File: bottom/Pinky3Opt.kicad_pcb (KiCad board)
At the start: 2 copper layers, 136 x 102.7 mm, 4 parts

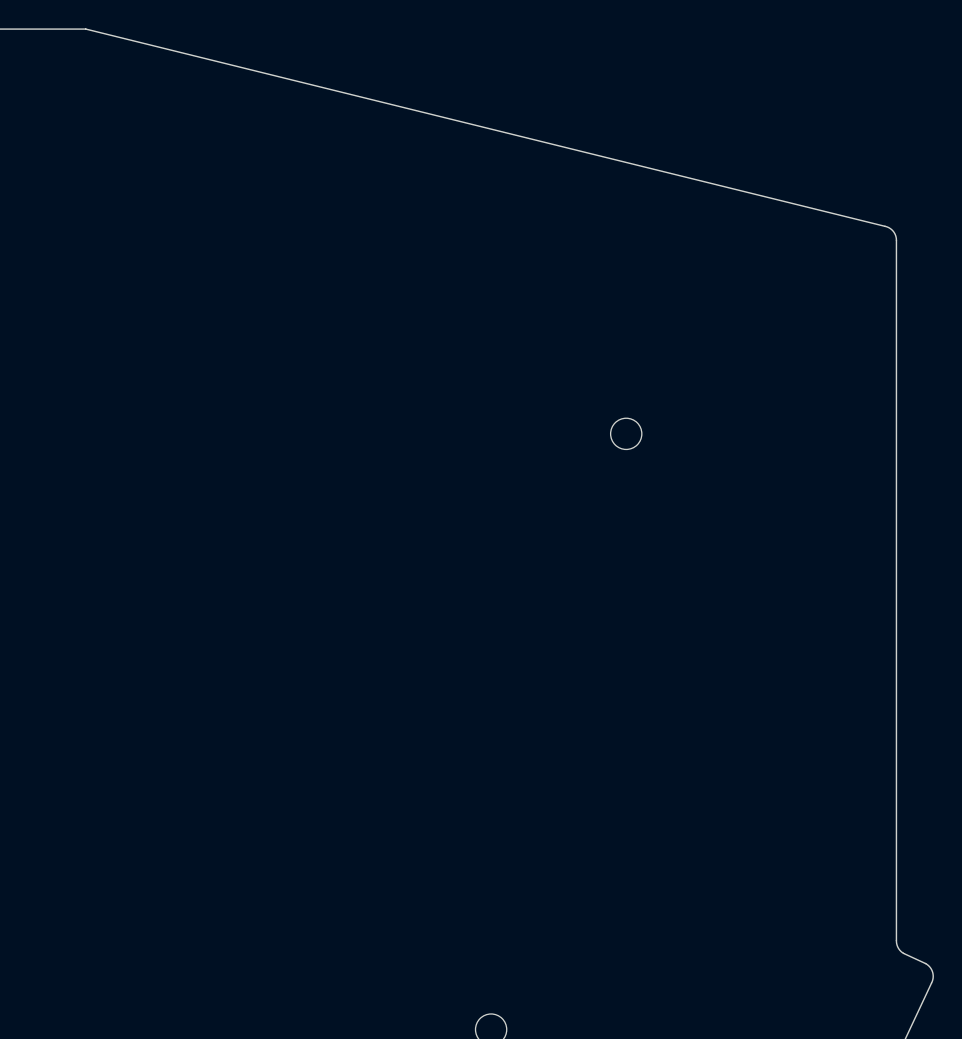
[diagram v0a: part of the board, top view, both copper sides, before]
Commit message: trrs bottom side
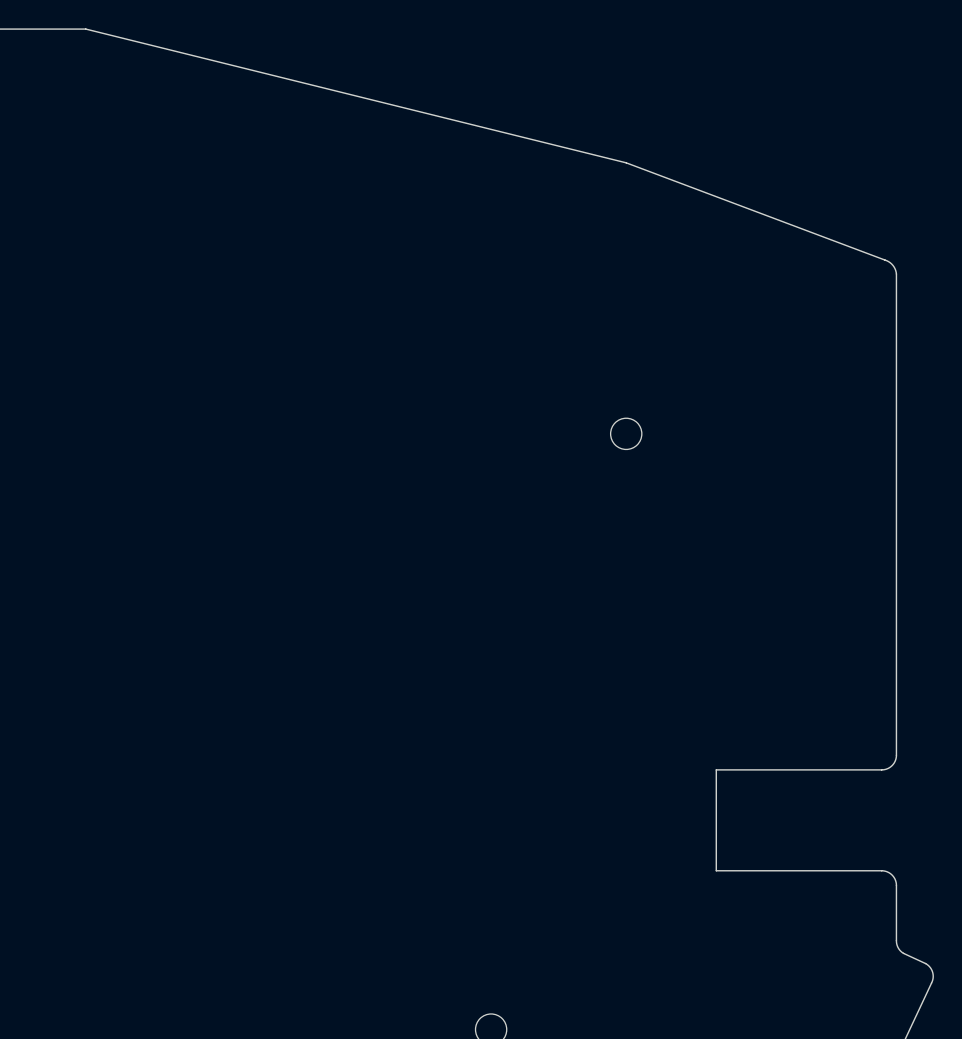
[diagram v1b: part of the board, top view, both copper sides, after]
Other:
- outline, holes or cut-outs redrawn
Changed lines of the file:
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@@
     (pad_to_mask_clearance 0)
     (pcbplotparams
-      (layerselection 0x00010fc_ffffffff)
+      (layerselection 0x00010f0_ffffffff)
       (plot_on_all_layers_selection 0x0000000_00000000)
       (disableapertmacros false)
@@
       (usegerberattributes true)
       (usegerberadvancedattributes true)
-      (creategerberjobfile true)
+      (creategerberjobfile false)
       (dashed_line_dash_ratio 12.000000)
       (dashed_line_gap_ratio 3.000000)
@@
       (outputformat 1)
       (mirror false)
-      (drillshape 1)
+      (drillshape 0)
       (scaleselection 1)
-      (outputdirectory "")
+      (outputdirectory "gerber")
     )
   )
@@
   (gr_line (start 140.275 137.53125) (end 124.225 131.65625)
     (stroke (width 0.1) (type default)) (layer "Edge.Cuts"))
-  (gr_arc (start 161.124548 56.801362) (mid 161.699451 57.148616) (end 161.925 57.78125)
+  (gr_arc (start 161.124548 59.182612) (mid 161.674565 59.550194) (end 161.925 60.1625)
     (stroke (width 0.1) (type default)) (layer "Edge.Cuts"))
   (gr_line (start 53.275 59.3) (end 64.45 56.5)
     (stroke (width 0.1) (type default)) (layer "Edge.Cuts"))
   (gr_arc (start 29.575001 114.316233) (mid 28.860834 114.020416) (end 28.565017 113.306249)
+    (stroke (width 0.1) (type default)) (layer "Edge.Cuts"))
+  (gr_arc (start 160.888049 102.235) (mid 161.621292 102.538709) (end 161.925 103.271953)
     (stroke (width 0.1) (type default)) (layer "Edge.Cuts"))
   (gr_arc (start 28.565017 57.834528) (mid 28.775003 57.206252) (end 29.322857 56.833855)
@@
   (gr_arc (start 163.979741 108.77574) (mid 164.475038 109.38125) (end 164.397041 110.159612)
     (stroke (width 0.1) (type default)) (layer "Edge.Cuts"))
-  (gr_line (start 104.775 42.89425) (end 161.124548 56.801362)
+  (gr_line (start 104.775 42.89425) (end 142.875 52.324)
     (stroke (width 0.1) (type default)) (layer "Edge.Cuts"))
   (gr_arc (start 86.8 114.316233) (mid 87.530604 114.618864) (end 87.833236 115.349476)
@@
   (gr_arc (start 157.016249 127.853355) (mid 156.591001 127.34925) (end 156.642241 126.69173)
     (stroke (width 0.1) (type default)) (layer "Edge.Cuts"))
-  (gr_line (start 161.925 57.78125) (end 161.925 107.163771)
+  (gr_line (start 161.925 60.1625) (end 161.925 94.087596)
     (stroke (width 0.1) (type default)) (layer "Edge.Cuts"))
   (gr_line (start 87.833237 127.687039) (end 87.833236 115.349476)
@@
   (gr_arc (start 88.845281 128.691681) (mid 88.133311 128.396821) (end 87.833237 127.687039)
     (stroke (width 0.1) (type default)) (layer "Edge.Cuts"))
+  (gr_line (start 142.875 52.324) (end 161.124548 59.182612)
+    (stroke (width 0.1) (type default)) (layer "Edge.Cuts"))
+  (gr_line (start 149.225 102.235) (end 160.888049 102.235)
+    (stroke (width 0.1) (type default)) (layer "Edge.Cuts"))
+  (gr_arc (start 161.925 94.087596) (mid 161.621741 94.819747) (end 160.889588 95.123)
+    (stroke (width 0.1) (type default)) (layer "Edge.Cuts"))
   (gr_line (start 162.425446 108.058064) (end 163.979741 108.77574)
     (stroke (width 0.1) (type default)) (layer "Edge.Cuts"))
-  (gr_arc (start 162.425446 108.058064) (mid 162.054378 107.678545) (end 161.925001 107.163771)
+  (gr_arc (start 162.42546 108.058041) (mid 162.054382 107.678536) (end 161.925001 107.163771)
     (stroke (width 0.1) (type default)) (layer "Edge.Cuts"))
   (gr_line (start 28.565017 113.306249) (end 28.565017 57.834528)
+    (stroke (width 0.1) (type default)) (layer "Edge.Cuts"))
+  (gr_line (start 161.925 103.271953) (end 161.925 107.163771)
     (stroke (width 0.1) (type default)) (layer "Edge.Cuts"))
   (gr_arc (start 155.382748 145.169705) (mid 154.73822 145.604553) (end 153.975 145.45625)
@@
   (gr_arc (start 50.264326 51.656195) (mid 51.075 51.775) (end 51.566311 52.430683)
     (stroke (width 0.1) (type default)) (layer "Edge.Cuts"))
+  (gr_line (start 160.889588 95.123) (end 149.225 95.123)
+    (stroke (width 0.1) (type default)) (layer "Edge.Cuts"))
   (gr_line (start 86.8 114.316233) (end 29.575001 114.316233)
     (stroke (width 0.1) (type default)) (layer "Edge.Cuts"))
+  (gr_line (start 149.225 95.123) (end 149.225 102.235)
+    (stroke (width 0.1) (type default)) (layer "Edge.Cuts"))
   (gr_line (start 124.225 131.65625) (end 107.375 128.691681)
